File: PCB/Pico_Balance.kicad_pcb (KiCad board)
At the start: 2 copper layers, 39 parts, among them J1 XT60PW-M, J2 GPIO_Ext, J3 Conn_Motor0, J4 Conn_Motor1, Q1 CSD17577Q3A, U1 BMI160, U2 DRV8876PWPR, U3 DRV8876PWPR, U4 LM74610QDGKRQ1, U5 LMR51430

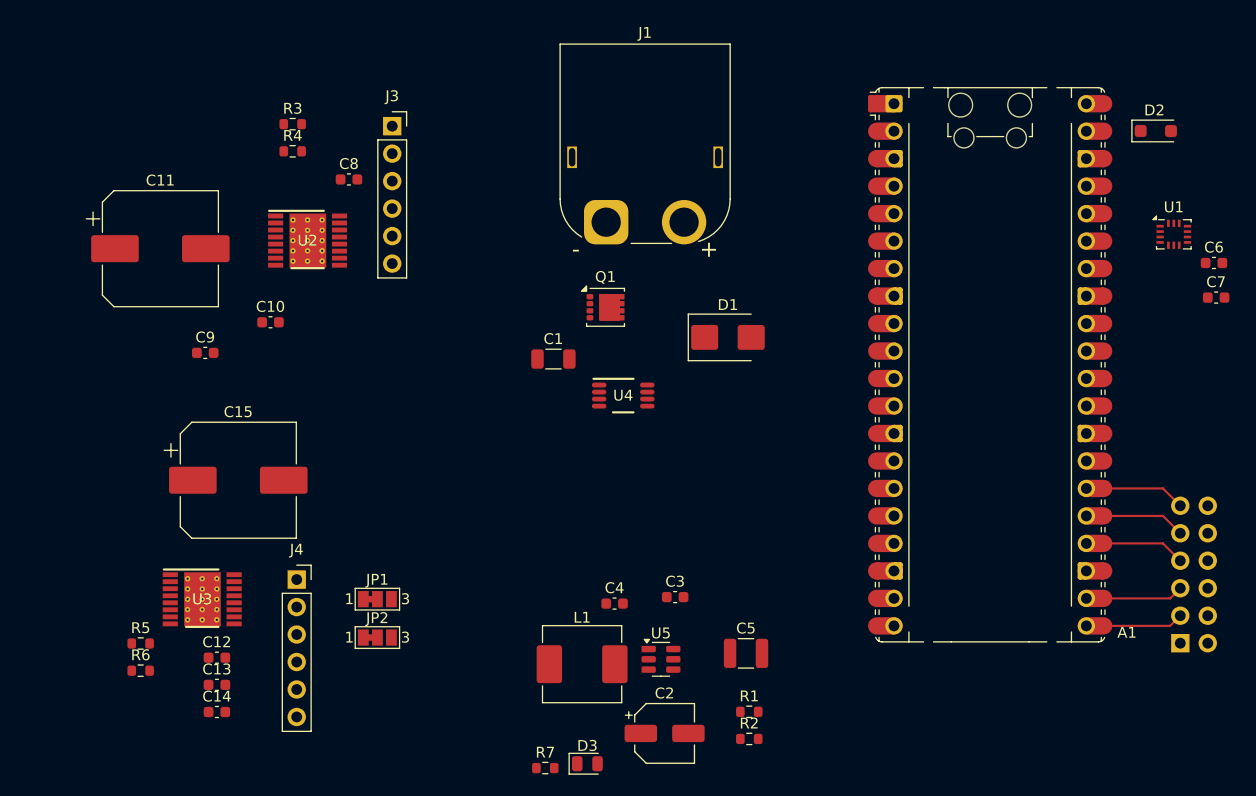
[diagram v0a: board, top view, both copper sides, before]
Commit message: Initial Input Protection Layout
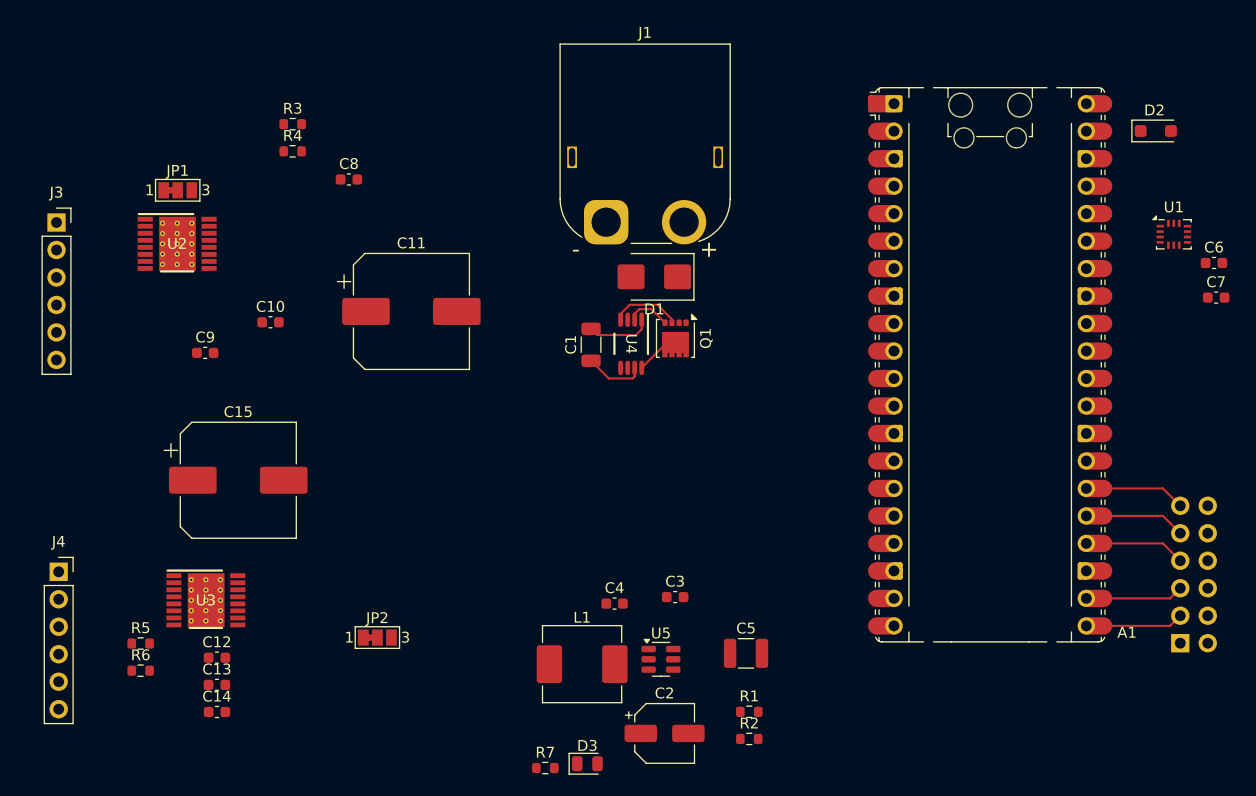
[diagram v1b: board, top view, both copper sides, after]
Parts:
- moved JP1 42.1 mm to (154.4, 85.0)
- moved J3 32.3 mm to (143.2, 88.0)
- moved C11 23.9 mm to (176.0, 96.2)
- moved J4 22.0 mm to (143.4, 120.3)
- moved U2 12.1 mm to (154.3, 90.0)
- moved D1 8.81 mm to (198.4, 93.0), turned to 180 degrees
- moved Q1 7.08 mm to (200.4, 98.7), turned to -90 degrees
- moved U4 4.84 mm to (196.3, 99.2), turned to -90 degrees
- moved C1 3.72 mm to (192.6, 99.3), turned to 90 degrees
- moved U3 0.35 mm to (157.0, 122.9)
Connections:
- Q1 pad 1: VM -> Net-(D1-A1)
- Q1 pad 2: VM -> Net-(D1-A1)
- Q1 pad 3: VM -> Net-(D1-A1)
- Q1 pad 5: Net-(D1-A1) -> VM
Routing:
- net Net-(D1-A1): track 0.00 -> 6.51 mm
- net Net-(U4-VCAPL): track 0.00 -> 6.02 mm
- net Net-(U4-VCAPH): track 0.00 -> 5.59 mm
- net VM: track 0.00 -> 4.09 mm
- net Net-(Q1-G): track 0.00 -> 4.05 mm

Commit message: Layout Refinements and add USB C port for power
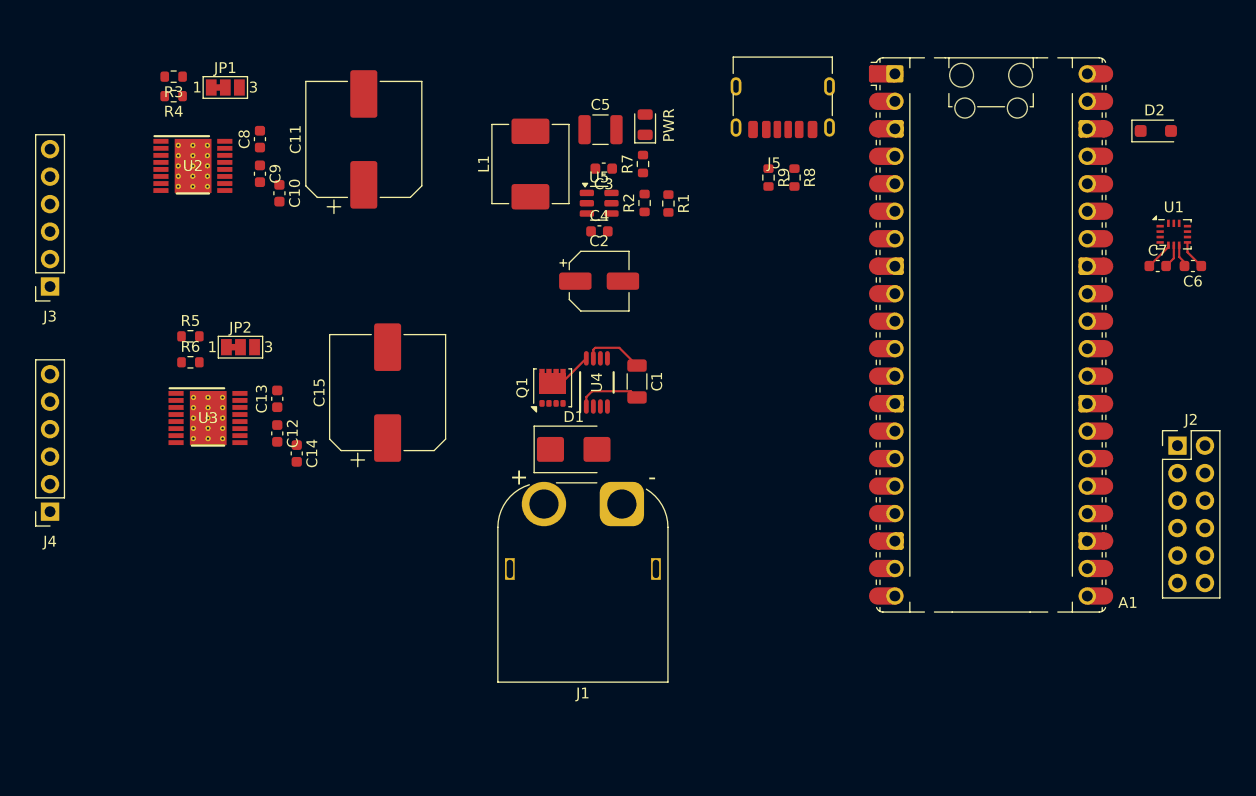
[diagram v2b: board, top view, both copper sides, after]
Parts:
- added J5: USB_C_Receptacle_PowerOnly_6P, Connector_USB:USB_C_Receptacle_HRO_TYPE-C-31-M-17, F.Cu at (210.3, 76.2)
- added R8: 10K, Resistor_SMD:R_0603_1608Metric, F.Cu at (211.4, 83.8)
- added R9: 10K, Resistor_SMD:R_0603_1608Metric, F.Cu at (209.0, 83.8)
- J2: moved to F.Cu
- moved PWR 59.3 mm to (197.6, 78.9), turned to 90 degrees
- moved R7 56.5 mm to (197.4, 82.6), turned to 90 degrees
- moved R2 50.5 mm to (197.6, 86.2), turned to 90 degrees
- moved C5 50.2 mm to (193.5, 79.4)
- moved R1 47.6 mm to (199.8, 86.2), turned to -90 degrees
- moved L1 46.5 mm to (187.0, 82.6), turned to 90 degrees
- moved U5 42.5 mm to (193.3, 86.2)
- moved C2 42.2 mm to (193.3, 93.4)
- moved C3 40.1 mm to (193.8, 83.0), turned to 180 degrees
- moved C4 34.4 mm to (193.4, 88.8)
- moved JP2 29.7 mm to (160.2, 99.5)
- moved R6 28.9 mm to (155.6, 100.9)
- moved R5 28.8 mm to (155.6, 98.5)
- moved C13 27.0 mm to (163.6, 104.3), turned to 90 degrees
- moved J1 26.1 mm to (195.4, 114.0), turned to 180 degrees
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- renumbered D3 to PWR
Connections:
- net Net-(A1-GPIO18) renamed GP18
- net Net-(U5-SW) renamed /SW
- A1 pad 21: Net-(A1-GPIO16) -> GP16
- A1 pad 22: Net-(A1-GPIO17) -> GP17
- A1 pad 25: Net-(A1-GPIO19) -> GP19
- A1 pad 26: Net-(A1-GPIO20) -> GP20
- J2 pad 11: Net-(A1-GPIO20) -> GP16
- J2 pad 3: Net-(A1-GPIO16) -> GP20
- J2 pad 5: Net-(A1-GPIO17) -> GP19
- J2 pad 9: Net-(A1-GPIO19) -> GP17
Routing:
- net Net-(A1-GPIO19): track 8.54 -> 0.00 mm
- net Net-(A1-GPIO20): track 8.54 -> 0.00 mm
- net GP18: track 8.54 -> 0.00 mm
- net Net-(A1-GPIO16): track 8.27 -> 0.00 mm
- net Net-(A1-GPIO17): track 8.27 -> 0.00 mm
- net Net-(D1-A1): track 6.51 -> 0.00 mm
- net +3V3: track 0.00 -> 5.36 mm
- net GND: track 0.00 -> 4.33 mm
- net Net-(Q1-G): track 4.05 -> 0.00 mm

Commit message: Layout Refinements
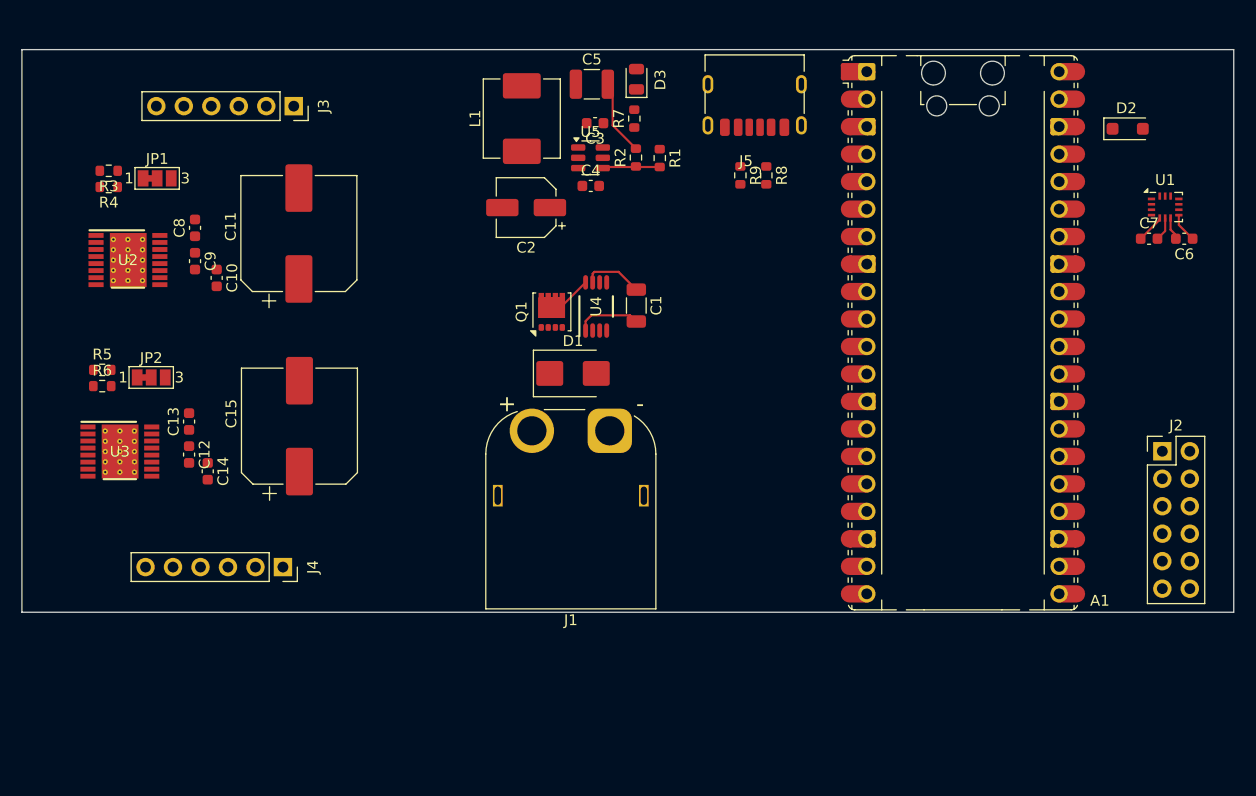
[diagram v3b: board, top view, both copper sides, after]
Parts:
- moved J3 28.0 mm to (165.1, 77.2), turned to -90 degrees
- moved J4 22.1 mm to (164.1, 119.8), turned to -90 degrees
- moved C11 10.6 mm to (165.6, 89.0)
- moved R3 10.6 mm to (148.0, 83.2)
- moved U2 10.6 mm to (149.8, 91.4)
- moved JP1 10.5 mm to (152.5, 83.9)
- moved R4 10.3 mm to (148.0, 84.7)
- moved C8 10.2 mm to (156.0, 88.5)
- moved C9 10.1 mm to (156.0, 91.5)
- moved C10 9.74 mm to (158.0, 93.1)
- moved C2 9.58 mm to (186.6, 86.6), turned to 180 degrees
- moved C15 8.72 mm to (165.7, 106.8)
- moved U3 8.72 mm to (149.1, 109.2)
- moved R5 8.72 mm to (147.4, 101.6)
- moved JP2 8.71 mm to (151.9, 102.3)
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- renumbered PWR to D3
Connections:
- A1 pad 10: ENCB0 -> SLP1
- A1 pad 14: SLP0 -> ENCA0
- A1 pad 15: SLP1 -> ENCB0
- A1 pad 9: ENCA0 -> SLP0
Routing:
- net GND: track 4.33 -> 11.4 mm
- net Net-(U5-FB): track 0.00 -> 5.30 mm
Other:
- board outline added: 112 x 52 mm

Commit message: First Round of Routing
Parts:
- moved R6 11.6 mm to (154.6, 112.2), turned to 90 degrees
- moved R4 11.6 mm to (154.6, 94.2), turned to 90 degrees
- moved C12 11.3 mm to (166.7, 110.7)
- moved C13 11.3 mm to (166.7, 107.6)
- moved C14 11.3 mm to (168.4, 112.2)
- moved U3 11.2 mm to (160.2, 110.4)
- moved C15 11.0 mm to (176.7, 107.0)
- moved C11 11.0 mm to (176.6, 89.0)
- moved C8 10.7 mm to (166.7, 89.5)
- moved C9 10.7 mm to (166.7, 92.5)
- moved C10 10.4 mm to (168.4, 94.1)
- moved U2 10.4 mm to (160.2, 92.4)
- moved R5 10.3 mm to (154.6, 109.0), turned to 90 degrees
- moved R3 10.2 mm to (154.6, 91.0), turned to 90 degrees
- moved JP2 10.1 mm to (161.9, 103.5)
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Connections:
- A1 pad 14: ENCA0 -> IN3
- A1 pad 15: ENCB0 -> IN4
- A1 pad 16: IN3 -> ENCA0
- A1 pad 17: IN4 -> ENCB0
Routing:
- net +3V3: track 5.36 -> 203.1 mm, vias 0 -> 2
- net CS0: track 0.00 -> 128.1 mm
- net ENCA0: track 0.00 -> 126.0 mm, vias 0 -> 1
- net ENCB0: track 0.00 -> 124.3 mm
- net +5V: track 0.00 -> 112.2 mm, vias 0 -> 1
- net CS1: track 0.00 -> 106.4 mm
- net SLP1: track 0.00 -> 81.3 mm, vias 0 -> 2
- net VM: track 4.09 -> 76.4 mm
- net IN2: track 0.00 -> 71.6 mm, vias 0 -> 2
- net SLP0: track 0.00 -> 70.1 mm, vias 0 -> 2
- net IN1: track 0.00 -> 69.6 mm, vias 0 -> 2
- net SDA: track 0.00 -> 67.8 mm, vias 0 -> 1
- net IN4: track 0.00 -> 67.6 mm, vias 0 -> 2
- net IN3: track 0.00 -> 66.4 mm, vias 0 -> 2
- net SCL: track 0.00 -> 63.7 mm, vias 0 -> 1
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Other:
- board size 112 x 52 mm -> 100 x 52 mm

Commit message: routing!!!!
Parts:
- turned R7 to -90 degrees
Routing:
- net Net-(Q1-G): track 0.00 -> 9.65 mm
- net Net-(D1-A1): track 5.98 -> 10.1 mm
- net Net-(D3-K): track 0.00 -> 1.96 mm
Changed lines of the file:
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@@
 	(footprint "Resistor_SMD:R_0603_1608Metric"
 		(layer "F.Cu")
-		(at 196.6 78.375 90)
+		(at 196.6 78.375 -90)
 		(descr "Resistor SMD 0603 (1608 Metric), square (rectangular) end terminal, IPC-7351 nominal, (Body size source: IPC-SM-782 page 72, https://www.pcb-3d.com/wordpress/wp-content/uploads/ipc-sm-782a_amendment_1_and_2.pdf), generated with kicad-footprint-generator")
 		(tags "resistor")
@@
 		(attr smd)
 		(fp_line
-			(start -0.237258 -0.5225)
-			(end 0.237258 -0.5225)
+			(start -0.237258 0.5225)
+			(end 0.237258 0.5225)
 			(stroke
 				(width 0.12)
@@
 		)
 		(fp_line
-			(start -0.237258 0.5225)
-			(end 0.237258 0.5225)
+			(start -0.237258 -0.5225)
+			(end 0.237258 -0.5225)
 			(stroke
 				(width 0.12)
@@
 		)
 		(fp_line
-			(start 1.48 -0.73)
-			(end 1.48 0.73)
+			(start -1.48 0.73)
+			(end -1.48 -0.73)
 			(stroke
 				(width 0.05)
@@
 		)
 		(fp_line
-			(start -1.48 -0.73)
-			(end 1.48 -0.73)
+			(start 1.48 0.73)
+			(end -1.48 0.73)
 			(stroke
 				(width 0.05)
@@
 		)
 		(fp_line
-			(start 1.48 0.73)
-			(end -1.48 0.73)
+			(start -1.48 -0.73)
+			(end 1.48 -0.73)
 			(stroke
 				(width 0.05)
@@
 		)
 		(fp_line
-			(start -1.48 0.73)
-			(end -1.48 -0.73)
+			(start 1.48 -0.73)
+			(end 1.48 0.73)
 			(stroke
 				(width 0.05)
@@
 		)
 		(fp_line
-			(start 0.8 -0.4125)
-			(end 0.8 0.4125)
+			(start -0.8 0.4125)
+			(end -0.8 -0.4125)
 			(stroke
 				(width 0.1)
@@
 		)
 		(fp_line
-			(start -0.8 -0.4125)
-			(end 0.8 -0.4125)
+			(start 0.8 0.4125)
+			(end -0.8 0.4125)
 			(stroke
 				(width 0.1)
@@
 		)
 		(fp_line
-			(start 0.8 0.4125)
-			(end -0.8 0.4125)
+			(start -0.8 -0.4125)
+			(end 0.8 -0.4125)
 			(stroke
 				(width 0.1)
@@
 		)
 		(fp_line
-			(start -0.8 0.4125)
-			(end -0.8 -0.4125)
+			(start 0.8 -0.4125)
+			(end 0.8 0.4125)
 			(stroke
 				(width 0.1)
@@
 		)
 		(pad "1" smd roundrect
-			(at -0.825 0 90)
+			(at -0.825 0 270)
 			(size 0.8 0.95)
 			(layers "F.Cu" "F.Mask" "F.Paste")
@@
 		)
 		(pad "2" smd roundrect
-			(at 0.825 0 90)
+			(at 0.825 0 270)
 			(size 0.8 0.95)
 			(layers "F.Cu" "F.Mask" "F.Paste")
@@
 	)
 	(segment
+		(start 188.7825 101.93)
+		(end 188.7825 101.1825)
+		(width 1.8)
+		(layer "F.Cu")
+		(net 55)
+	)
+	(segment
 		(start 188.7825 105.58)
 		(end 187.1325 107.23)
@@
 	)
 	(segment
+		(start 188.5915 100.9915)
+		(end 188.5915 97.911)
+		(width 1.8)
+		(layer "F.Cu")
+		(net 55)
+	)
+	(segment
 		(start 188.7825 101.93)
 		(end 188.7825 105.58)
@@
 	)
 	(segment
+		(start 188.7825 101.1825)
+		(end 188.5915 100.9915)
+		(width 1.8)
+		(layer "F.Cu")
+		(net 55)
+	)
+	(segment
+		(start 196.8 75.675)
+		(end 196.8 77.35)
+		(width 0.2)
+		(layer "F.Cu")
+		(net 56)
+	)
+	(segment
+		(start 196.8 77.35)
+		(end 196.6 77.55)
+		(width 0.2)
+		(layer "F.Cu")
+		(net 56)
+	)
+	(segment
 		(start 164.132071 94.075)
 		(end 164.207072 94.150001)
@@
 	)
 	(segment
+		(start 189.9425 97.68)
+		(end 193.397501 94.224999)
+		(width 0.2)
+		(layer "F.Cu")
+		(net 61)
+	)
+	(segment
+		(start 192.315377 98.940999)
+		(end 192.747502 98.508874)
+		(width 0.2)
+		(layer "F.Cu")
+		(net 61)
+	)
+	(segment
+		(start 192.747502 98.508874)
+		(end 192.747502 97.964999)
+		(width 0.2)
+		(layer "F.Cu")
+		(net 61)
+	)
+	(segment
+		(start 189.9425 97.68)
+		(end 191.203499 98.940999)
+		(width 0.2)
+		(layer "F.Cu")
+		(net 61)
+	)
+	(segment
+		(start 191.203499 98.940999)
+		(end 192.315377 98.940999)
+		(width 0.2)
+		(layer "F.Cu")
+		(net 61)
+	)
+	(segment
+		(start 193.397501 94.224999)
+		(end 193.397501 93.514998)
+		(width 0.2)
+		(layer "F.Cu")
+		(net 61)
+	)
+	(segment

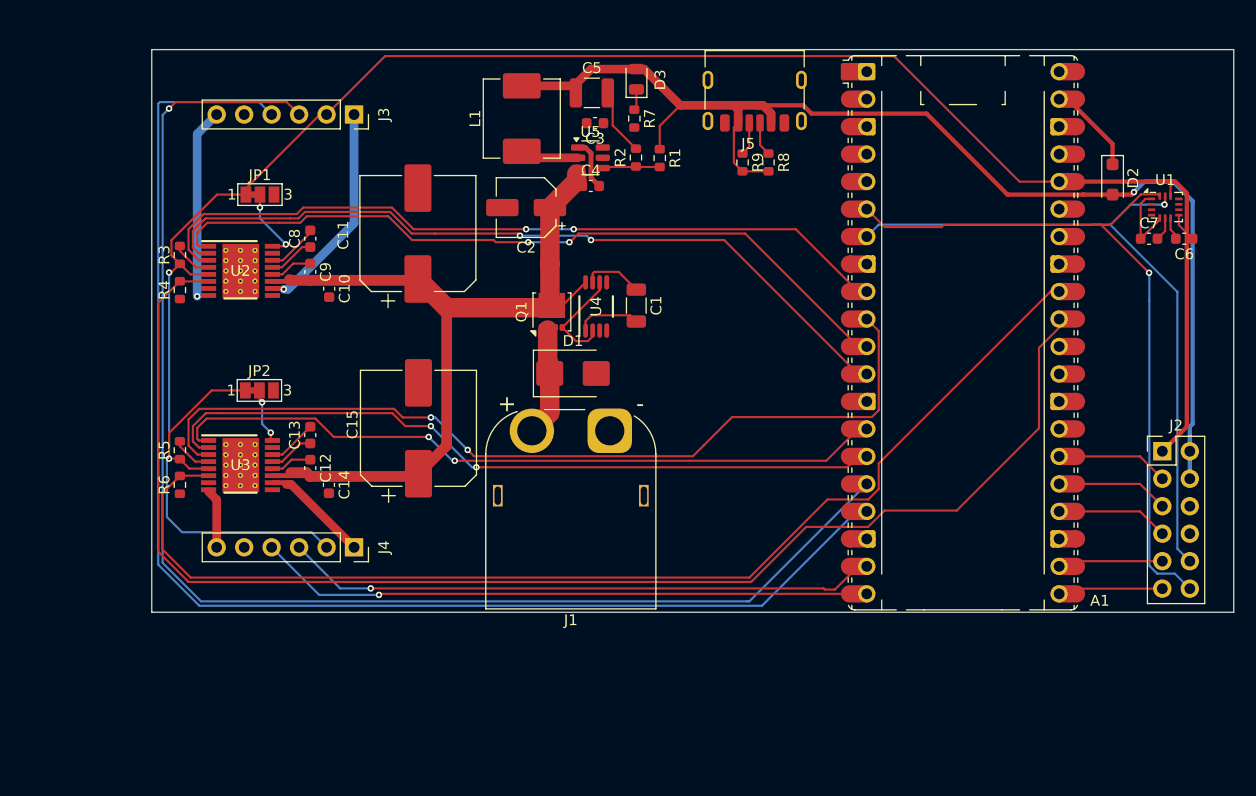
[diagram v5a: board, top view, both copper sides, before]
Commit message: Routing refinement and pour ground planes
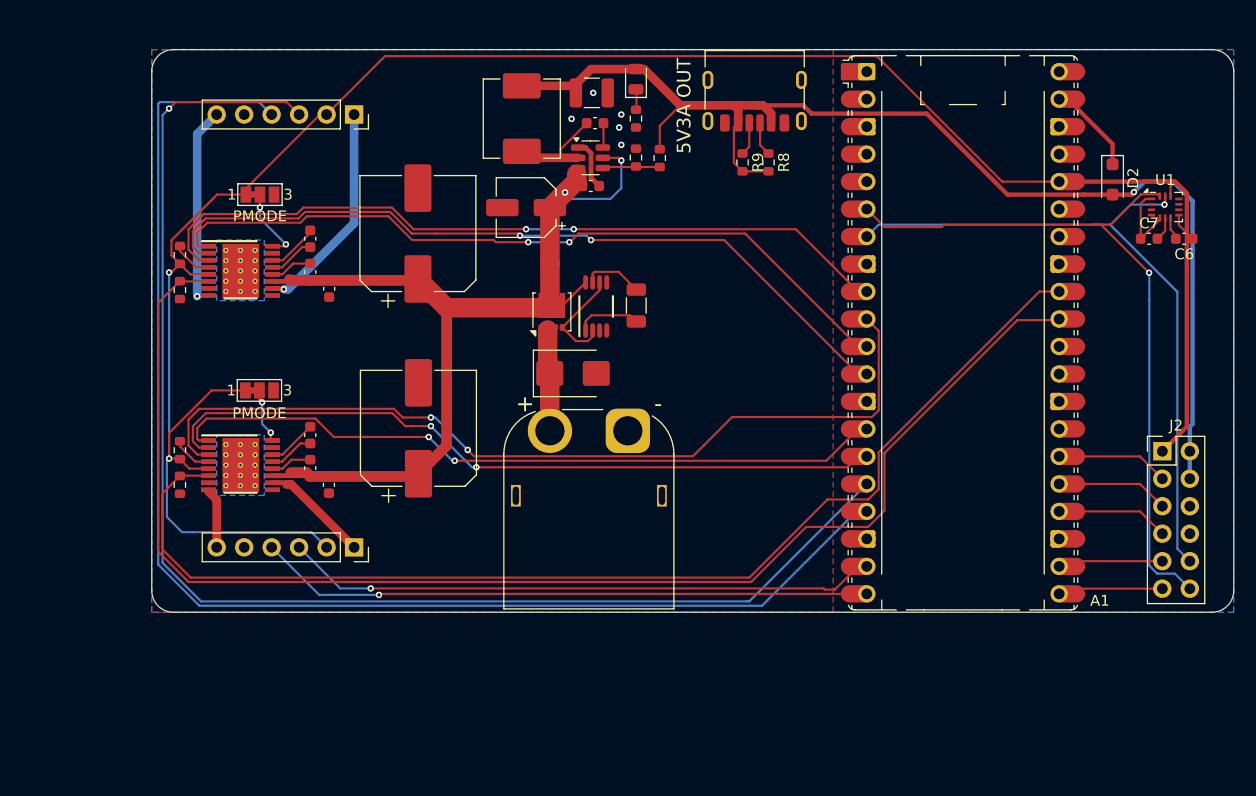
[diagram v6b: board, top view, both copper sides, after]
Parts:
- J5: value USB_C_Receptacle_PowerOnly_6P -> 5V3A OUT
- JP1, JP2: value SolderJumper_3_Bridged12 -> PMODE
- moved J1 1.67 mm to (196.0, 107.2)
- moved R7 0.15 mm to (196.8, 78.4)
- moved D3 0.05 mm to (196.8, 74.7)
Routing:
- net VM: track 76.4 -> 86.6 mm, vias 0 -> 2
- net GND: track 15.3 -> 10.0 mm, vias 0 -> 5
- net /SW: track 5.46 -> 9.66 mm
- net Net-(U5-CB): track 0.00 -> 2.28 mm
- net CS0: track 128.1 -> 126.9 mm
- net Net-(D1-A1): track 10.1 -> 9.41 mm
- net CS1: track 106.4 -> 107.0 mm
- added copper zone on B.Cu, net GND
- added copper zone on F.Cu, net GND
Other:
- outline, holes or cut-outs redrawn
